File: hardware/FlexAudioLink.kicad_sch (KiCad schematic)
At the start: 20 parts, among them J1 USB_C_Receptacle_USB2.0_14P, Q1 FDS9926A, U1 TPS631000, U2 DW01A, U3 TP4056-42-ESOP8

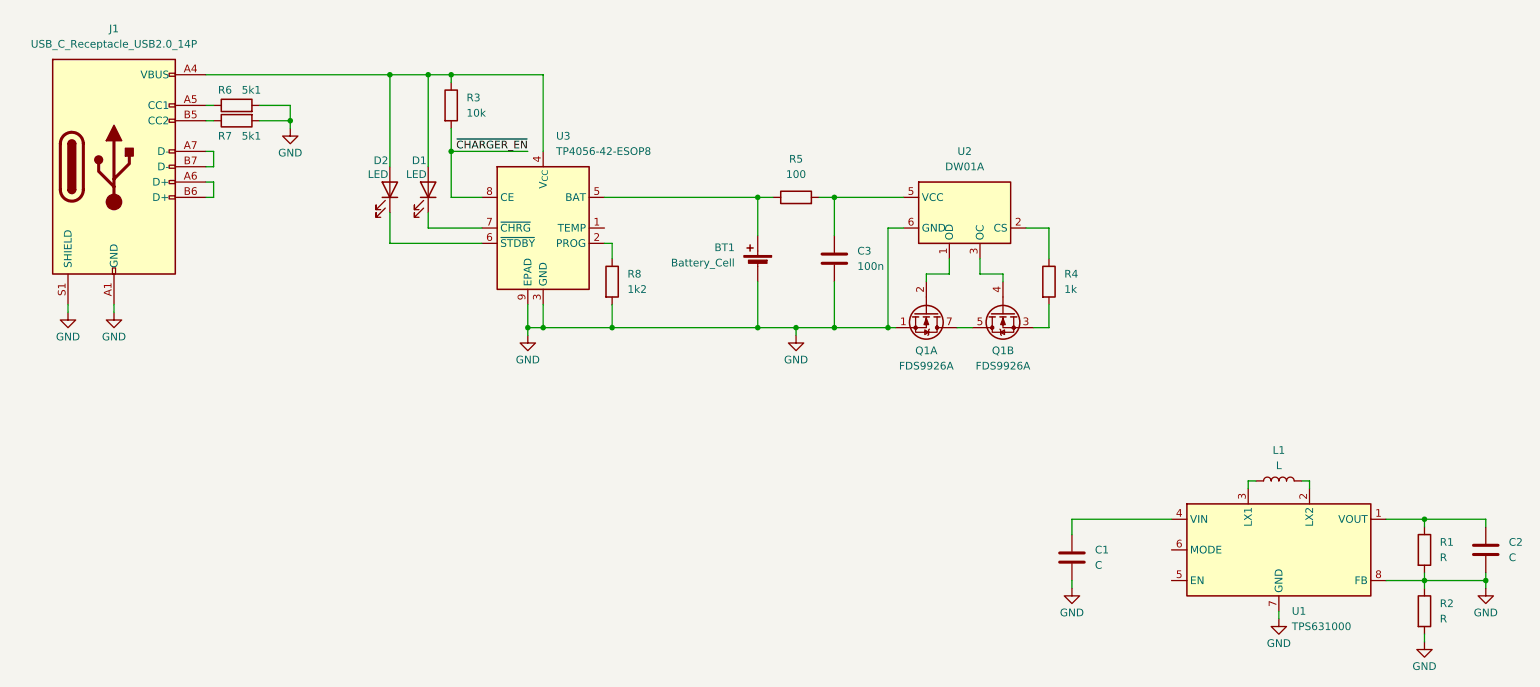
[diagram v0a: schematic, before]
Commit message: Add RW612 Symbol, HVQFN116 footprint & 3D Model; Organize schematic into two sheets with top level sheet;
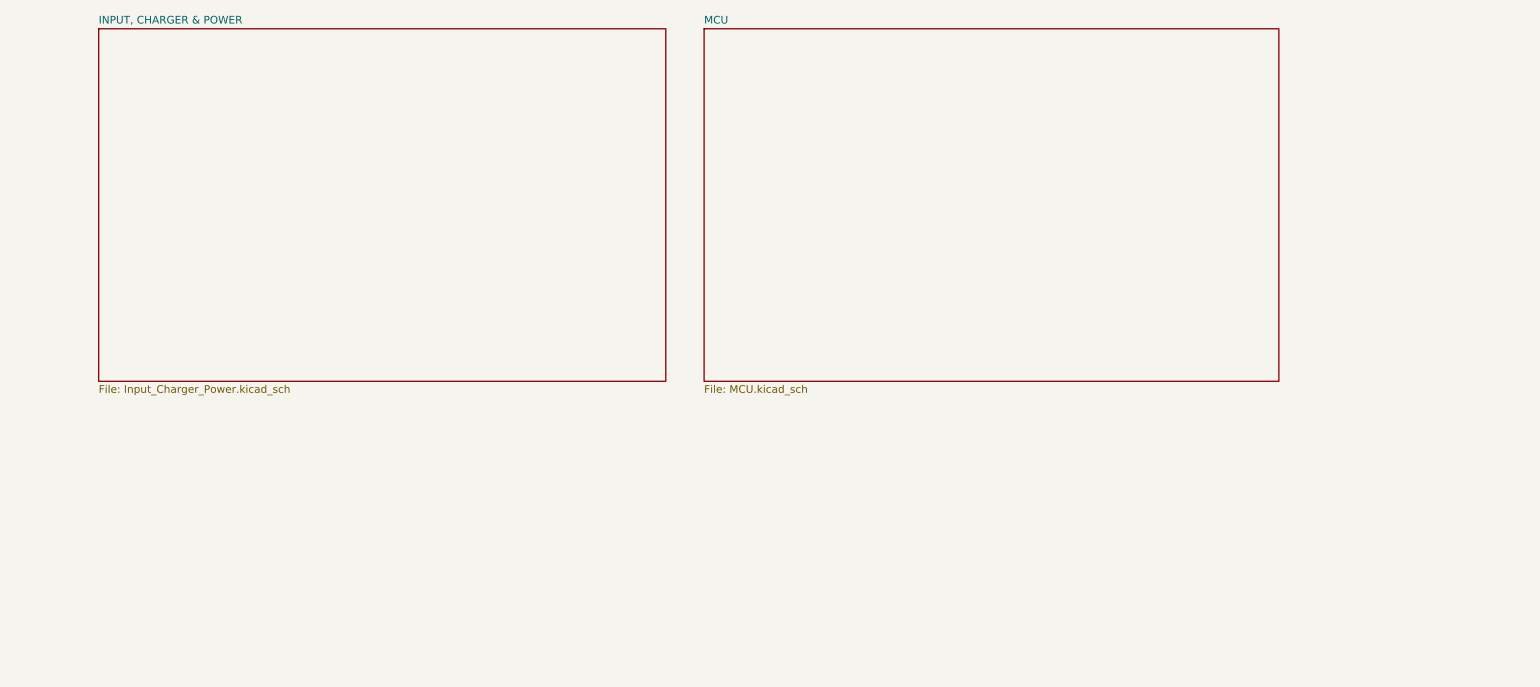
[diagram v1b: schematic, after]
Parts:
- removed BT1: Battery_Cell, symbol Device:Battery_Cell
- removed C1, C2: C, symbol Device:C
- removed C3: 100n, symbol Device:C
- removed D1, D2: LED, symbol Device:LED
- removed J1: USB_C_Receptacle_USB2.0_14P, symbol Connector:USB_C_Receptacle_USB2.0_14P
- removed L1: L, symbol Device:L
- removed Q1: FDS9926A, Package_SO:SOIC-8_3.9x4.9mm_P1.27mm, symbol Transistor_FET:FDS9926A
- removed R1, R2: R, symbol Device:R
- removed R3: 10k, symbol Device:R
- removed R4: 1k, symbol Device:R
- removed R5: 100, symbol Device:R
- removed R6, R7: 5k1, symbol Device:R
- removed R8: 1k2, symbol Device:R
- removed U1: TPS631000, Package_TO_SOT_SMD:SOT-583-8, symbol FlexAudioLink_Symbols:TPS631000
- removed U2: DW01A, Package_TO_SOT_SMD:SOT-23-6, symbol Battery_Management:DW01A
- removed U3: TP4056-42-ESOP8, Package_SO:SOIC-8-1EP_3.9x4.9mm_P1.27mm_EP2.41x3.3mm_ThermalVias, symbol Battery_Management:TP4056-42-ESOP8
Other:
- added sheet INPUT, CHARGER & POWER (Input_Charger_Power.kicad_sch)
- added sheet MCU (MCU.kicad_sch)
